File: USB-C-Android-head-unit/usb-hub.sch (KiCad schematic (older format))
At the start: 1 part

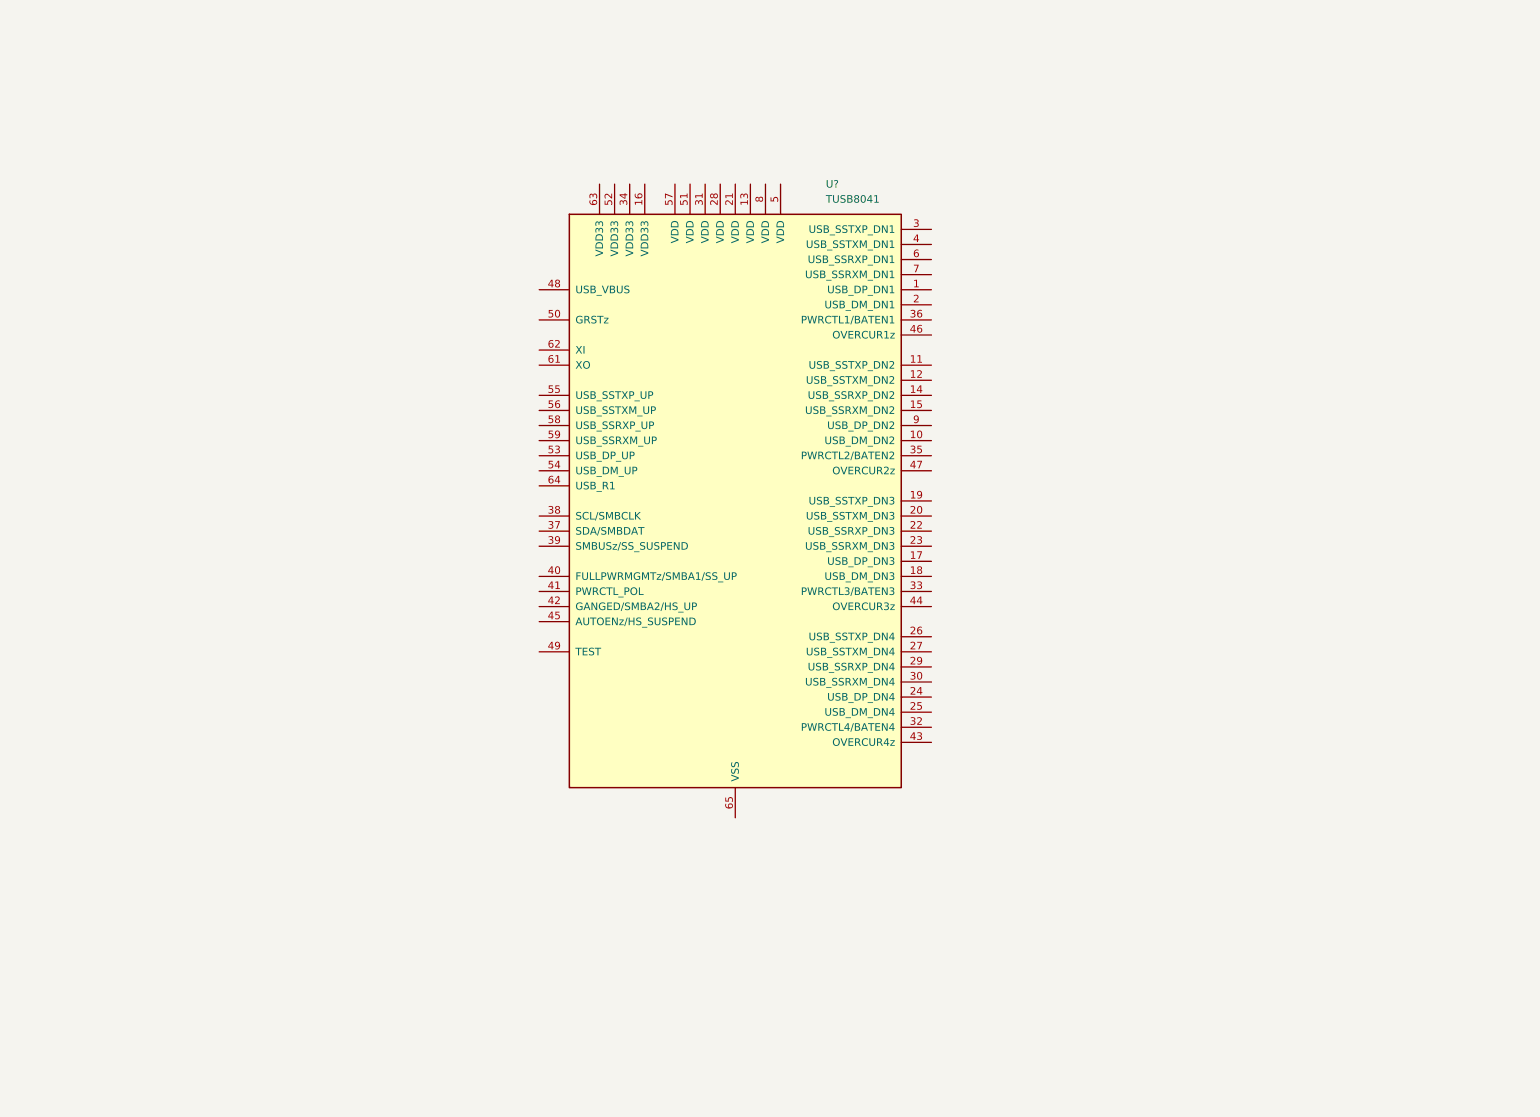
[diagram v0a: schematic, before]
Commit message: work on USB hub
Also changed sheet sizes
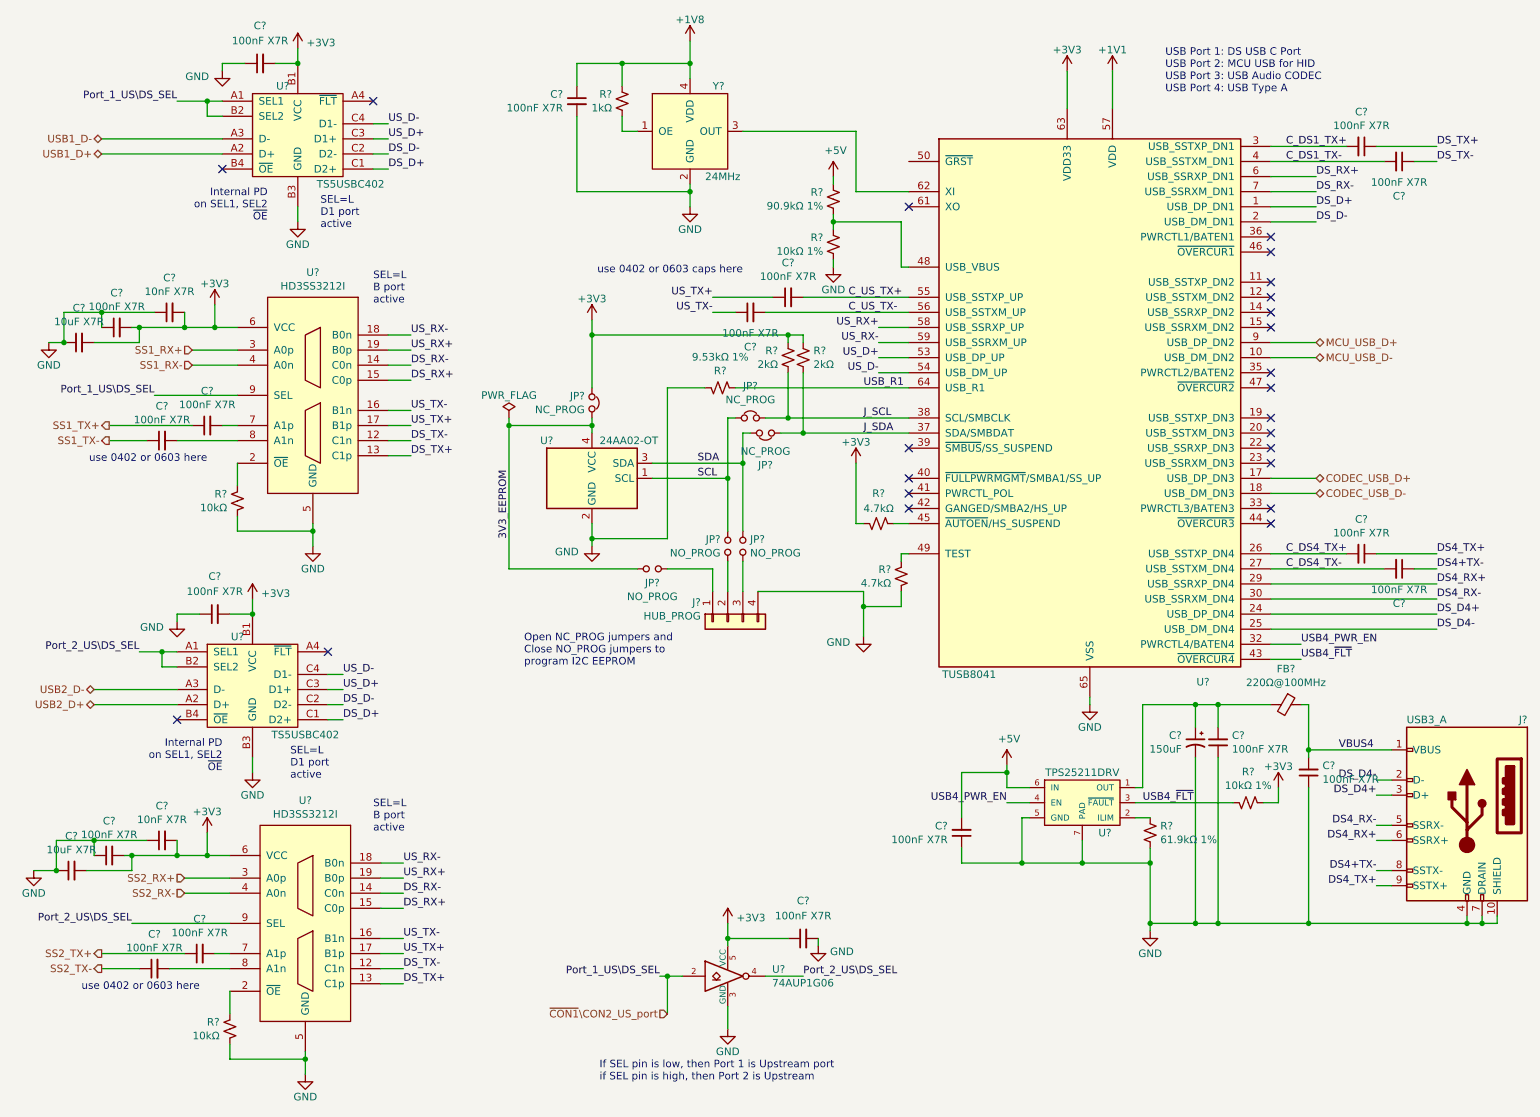
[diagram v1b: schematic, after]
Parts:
- removed U?: TUSB8041, Package_DFN_QFN:QFN-64-1EP_9x9mm_P0.5mm_EP6x6mm_ThermalVias, symbol Interface_USB:TUSB8041
- added C? (x19): 100nF X7R, symbol Device:C_Small
- added C? (x2): 10nF X7R, symbol Device:C_Small
- added C? (x2): 10uF X7R, symbol Device:C_Small
- added C?: 150uF, symbol Device:CP1_Small
- added FB?: 220Ω@100MHz, Resistor_SMD:R_0603_1608Metric, symbol Device:Ferrite_Bead_Small
- added J?: HUB_PROG, symbol Connector_Generic:Conn_01x04
- added J?: USB3_A, symbol Connector:USB3_A
- added JP? (x3): NC_PROG, symbol Device:Jumper_NC_Small
- added JP? (x3): NO_PROG, symbol Device:Jumper_NO_Small
- added R? (x2): 10kΩ, symbol Device:R_Small_US
- added R?: 90.9kΩ 1%, symbol Device:R_Small_US
- added R? (x2): 10kΩ 1%, symbol Device:R_Small_US
- added R?: 1kΩ, symbol Device:R_Small_US
- added R?: 9.53kΩ 1%, symbol Device:R_Small_US
- added R? (x2): 4.7kΩ, symbol Device:R_Small_US
- added R? (x2): 2kΩ, symbol Device:R_Small_US
- added R?: 61.9kΩ 1%, symbol Device:R_Small_US
- added U? (x2): HD3SS3212I, symbol SW-Texas:HD3SS3212I
- added U?: TUSB8041, Package_DFN_QFN:QFN-64-1EP_9x9mm_P0.5mm_EP6x6mm_ThermalVias, symbol SW-Texas:TUSB8041
- added U?: 24AA02-OT, Package_TO_SOT_SMD:SOT-353_SC-70-5, symbol Memory_EEPROM:24AA02-OT
- added U?: TPS25211DRV, Package_SON:WSON-6-1EP_2x2mm_P0.65mm_EP1x1.6mm_ThermalVias, symbol SW-Texas:TPS25211DRV
- added U? (x2): TS5USBC402, symbol SW-Texas:TS5USBC402
- added U?: 74AUP1G06, symbol 74xGxx:74AUP1G06
- added Y?: 24MHz, symbol SW-SiTime:SiT1602B
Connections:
- new net: R?.1, U?.2 (~OE) (x2)
- new net: C?.2, U?.7 (A1p) (x2)
- new net: C?.2, U?.8 (A1n) (x2)
- new net: R?.2, U?.45 (~AUTOEN~/HS_SUSPEND)
- new net: R?.1, R?.2, U?.48 (USB_VBUS)
- new net: R?.2, U?.49 (TEST)
- new net: U?.62 (XI), Y?.3 (OUT)
- new net: R?.2, Y?.1 (OE)
- new net: J?.2 (Pin_2), JP?.1
- new net: J?.3 (Pin_3), JP?.1
- new net: J?.1 (Pin_1), JP?.2
- new net: C?.1, C?.2, FB?.2, U?.1 (OUT)
- new net: R?.2, U?.2 (ILIM)
- new net +1V1: U?.13 (VDD), U?.21 (VDD), U?.28 (VDD), U?.31 (VDD), U?.5 (VDD), U?.51 (VDD), U?.57 (VDD), U?.8 (VDD)
- new net +1V8: C?.1, R?.1, Y?.4 (VDD)
- new net +3V3: C?.1, C?.2, C?.2, C?.2, C?.2, C?.2, C?.2, C?.2, C?.2, JP?.1, R?.1, R?.1, R?.1, R?.1, U?.16 (VDD33), U?.34 (VDD33), U?.5 (VCC), U?.52 (VDD33), U?.6 (VCC), U?.6 (VCC), U?.63 (VDD33), U?.B1 (VCC), U?.B1 (VCC)
- new net +5V: C?.2, R?.1, U?.6 (IN)
- new net 3V3_EEPROM: JP?.1, JP?.2, U?.4 (VCC)
- new net CODEC_USB_D+: U?.17 (USB_DP_DN3)
- new net CODEC_USB_D-: U?.18 (USB_DM_DN3)
- new net C_DS1_TX+: C?.2, U?.3 (USB_SSTXP_DN1)
- new net C_DS1_TX-: C?.2, U?.4 (USB_SSTXM_DN1)
- new net C_DS4_TX+: C?.2, U?.26 (USB_SSTXP_DN4)
- new net C_DS4_TX-: C?.2, U?.27 (USB_SSTXM_DN4)
- new net C_US_TX+: C?.2, U?.55 (USB_SSTXP_UP)
- new net C_US_TX-: C?.2, U?.56 (USB_SSTXM_UP)
- new net DS4+TX-: C?.1, J?.8 (SSTX-)
- new net DS4_RX+: J?.6 (SSRX+), U?.29 (USB_SSRXP_DN4)
- new net DS4_RX-: J?.5 (SSRX-), U?.30 (USB_SSRXM_DN4)
- new net DS4_TX+: C?.1, J?.9 (SSTX+)
- new net DS_D+: U?.1 (USB_DP_DN1), U?.C1 (D2+), U?.C1 (D2+)
- new net DS_D-: U?.2 (USB_DM_DN1), U?.C2 (D2-), U?.C2 (D2-)
- new net DS_D4+: J?.3 (D+), U?.24 (USB_DP_DN4)
- new net DS_D4-: J?.2 (D-), U?.25 (USB_DM_DN4)
- new net DS_RX+: U?.15 (C0p), U?.15 (C0p), U?.6 (USB_SSRXP_DN1)
- new net DS_RX-: U?.14 (C0n), U?.14 (C0n), U?.7 (USB_SSRXM_DN1)
- new net DS_TX+: C?.1, U?.13 (C1p), U?.13 (C1p)
- new net DS_TX-: C?.1, U?.12 (C1n), U?.12 (C1n)
- new net GND: C?.1, C?.1, C?.1, C?.1, C?.1, C?.1, C?.1, C?.1, C?.1, C?.1, C?.1, C?.2, C?.2, C?.2, J?.10 (SHIELD), J?.4 (GND), J?.4 (Pin_4), J?.7 (DRAIN), R?.1, R?.1, R?.2, R?.2, R?.2, R?.2, U?.11 (GND), U?.11 (GND), U?.2 (GND), U?.20 (GND), U?.20 (GND), U?.3 (GND), U?.5 (GND), U?.5 (GND), U?.5 (GND), U?.65 (VSS), U?.7 (PAD), U?.B3 (GND), U?.B3 (GND), Y?.2 (GND)
- new net J_SCL: JP?.2, R?.2, U?.38 (SCL/SMBCLK)
- new net J_SDA: JP?.2, R?.2, U?.37 (SDA/SMBDAT)
- new net MCU_USB_D+: U?.9 (USB_DP_DN2)
- new net MCU_USB_D-: U?.10 (USB_DM_DN2)
- new net Port_2_US\DS_SEL: U?.4, U?.9 (SEL), U?.A1 (SEL1), U?.B2 (SEL2)
- new net SCL: JP?.1, JP?.2, U?.1 (SCL)
- new net SDA: JP?.1, JP?.2, U?.3 (SDA)
- new net SS1_RX+: U?.3 (A0p)
- new net SS1_RX-: U?.4 (A0n)
- new net SS1_TX+: C?.1
- new net SS1_TX-: C?.1
- new net SS2_RX+: U?.3 (A0p)
- new net SS2_RX-: U?.4 (A0n)
- new net SS2_TX+: C?.1
- new net SS2_TX-: C?.1
- new net USB1_D+: U?.A2 (D+)
- new net USB1_D-: U?.A3 (D-)
- new net USB2_D+: U?.A2 (D+)
- new net USB2_D-: U?.A3 (D-)
- new net USB4_PWR_EN: U?.32 (PWRCTL4/BATEN4), U?.4 (EN)
- new net USB4_~FLT~: R?.2, U?.3 (~FAULT), U?.43 (~OVERCUR4)
- new net USB_R1: R?.1, U?.64 (USB_R1)
- new net US_D+: U?.53 (USB_DP_UP), U?.C3 (D1+), U?.C3 (D1+)
- new net US_D-: U?.54 (USB_DM_UP), U?.C4 (D1-), U?.C4 (D1-)
- new net US_RX+: U?.19 (B0p), U?.19 (B0p), U?.58 (USB_SSRXP_UP)
- new net US_RX-: U?.18 (B0n), U?.18 (B0n), U?.59 (USB_SSRXM_UP)
- new net US_TX+: C?.1, U?.17 (B1p), U?.17 (B1p)
- new net US_TX-: C?.1, U?.16 (B1n), U?.16 (B1n)
- new net VBUS4: C?.2, FB?.1, J?.1 (VBUS)
- new net ~CON1~\CON2_US_port: U?.2, U?.9 (SEL), U?.A1 (SEL1), U?.B2 (SEL2)
- no-connect marks 0 -> 23
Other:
- note added: "If SEL pin is low, then Port 1 is Upstream port\nif SEL pin is high, then Port 2 is Upstream"
- note added: "Internal PD\non SEL1, SEL2\n~OE~"
- note added: "Open NC_PROG jumpers and\nClose NO_PROG jumpers to\nprogram I2C EEPROM"
- note added: "SEL=L\nB port\nactive"
- note added: "SEL=L\nD1 port\nactive"
- note added: "USB Port 1: DS USB C Port\nUSB Port 2: MCU USB for HID\nUSB Port 3: USB Audio CODEC\nUSB Port 4: USB Type A"
- note added: "use 0402 or 0603 caps here"
- note added: "use 0402 or 0603 here"
